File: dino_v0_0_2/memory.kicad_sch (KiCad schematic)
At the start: 15 parts, among them U19 74LS245, U21 74LS245, U24 AT28C256, U26 MCM60256AP, U51 7400, U74 74LS00, U75 74LS32

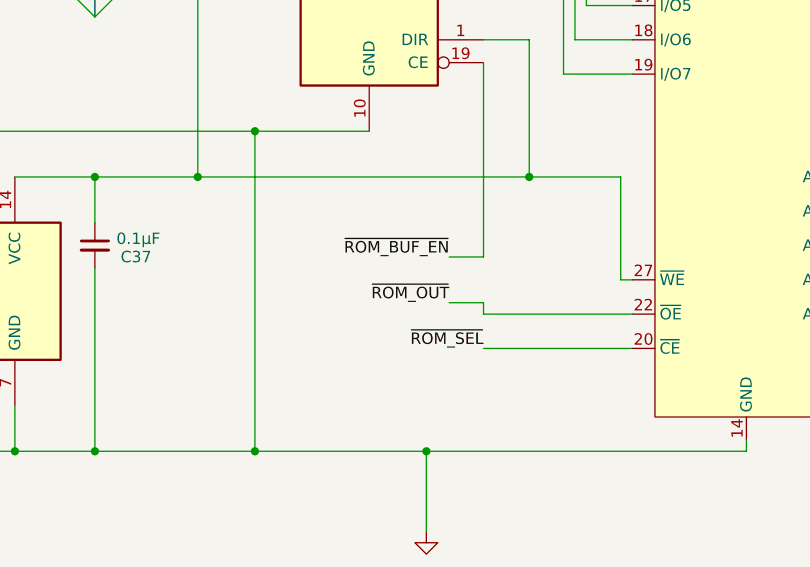
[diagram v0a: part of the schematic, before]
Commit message: feat: phase G_0 on silicon -- ROM readable as data, monitor runs its session
Three re-sourced pins make ROM readable as data (PROG_test3 0x4D, romsoak
0x00 over 65536 reads). The monitor then runs the session from the ask:
D 0000 -> 0x11, W FF00,99 -> 0x99, D FF00 -> 0x99, O FF00 on OB.

Four faults sat between the copper and that session, all fixed, all in
.git/sdd/PHASE_G_0.md RESULTS:

1. U15 (microcode EEPROM, CW8-15) pulsed END on its own for ~25ns with a
   static address, clean rails and ~OE/~CE low, locked to no clock in the
   machine. U61 turned it into ~MR low, U6 cleared T under HALT, and the
   byte behind the HALT ran. Every "HALT escape" ever recorded was this.
   Chip replaced; same image; no pulses.
2. MVI/MVIX/MVIS parked the immediate on a bus fight: CW14 flipped M to
   MAR before the source decode retired ~ROM_OUT, FETCH_RAM fired, and the
   RAM drove the cell's old byte under U18's open latch. PROG_isa was blind
   to it (PLANT rewrites the same 0x2E). Settle row with pc_up on the
   settle, not the park. Burned: U9 0xC52B  U15 0xDCD1  U23 0xCB8E.
3. LE_MDR opened on ~RAM_LOAD during the replay row. U39.4 strapped +5V;
   LE_MDR = NOT(READS_IDLE).
4. The spec's RAM-side wire (U74.9 <- READ) was identical logic and three
   gates faster on M15, which made fault 2 deterministic. Reverted to
   RAM_OE_ON.

Schematic matches copper: --since HEAD reads copper 3 (U22.11, U24.22,
U39.4), annotate 2; ERC delta -2, none new.

Tooling: asm/wander (ten slots, escape ladder), test4, test5 (six-slot
bisection), romsoak (ROM-as-data x65536, OB = misses), answer keys for
each; make gen-isa and burn-prog-isa; progrom_gen no longer writes over
asm-owned images; test_no_rom_park_flips_M_before_the_latch_closes.

OPEN: first ~3 data reads after POWER-UP miss, five witnesses in the doc.

Co-Authored-By: Claude Fable 5.1 <noreply@anthropic.com>
Claude-Session: https://claude.ai/code/session_01QTZogB99di5hEgzEycbhhD
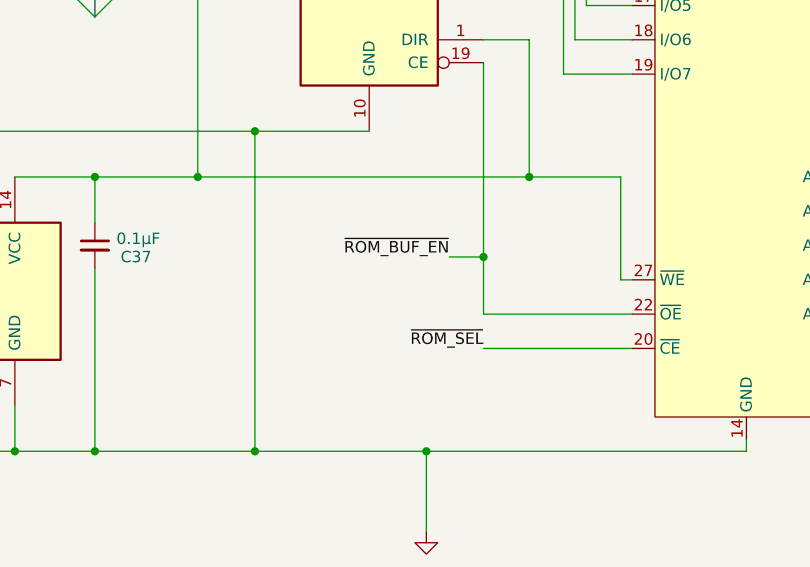
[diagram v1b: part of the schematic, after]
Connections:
- net ~{ROM_OUT} is gone; now on net ~{ROM_BUF_EN}: U24.22 (~{OE})
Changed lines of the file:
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@@
+	)
+	(junction
+		(at 200.66 90.17)
+		(diameter 0)
+		(color 0 0 0 0)
 	)
 	(junction
@@
 	(wire
 		(pts
-			(xy 196.85 95.25) (xy 200.66 95.25)
-		)
-		(stroke
-			(width 0)
-			(type default)
-		)
-	)
-	(wire
-		(pts
 			(xy 100.33 62.23) (xy 105.41 62.23)
 		)
@@
 	(wire
 		(pts
-			(xy 200.66 95.25) (xy 200.66 96.52)
+			(xy 200.66 90.17) (xy 200.66 96.52)
 		)
 		(stroke
@@
 		)
 	)
+	(label "RAM_OE_ON"
+		(at 26.67 175.26 180)
+		(effects
+			(font
+				(size 1.27 1.27)
+			)
+			(justify right bottom)
+		)
+	)
 	(label "MDR1"
 		(at 160.02 45.72 0)
@@
 		)
 	)
-	(label "~{ROM_OUT}"
-		(at 196.85 95.25 180)
-		(effects
-			(font
-				(size 1.27 1.27)
-			)
-			(justify right bottom)
-		)
-	)
 	(label "MDR5"
 		(at 154.94 55.88 180)
@@
 		(effects
 			(font
-				(size 1.27 1.27)
-			)
-			(justify right bottom)
-		)
-	)
-	(label "RAM_OE_ON"
-		(at 26.67 175.26 180)
-		(effects
-			(font

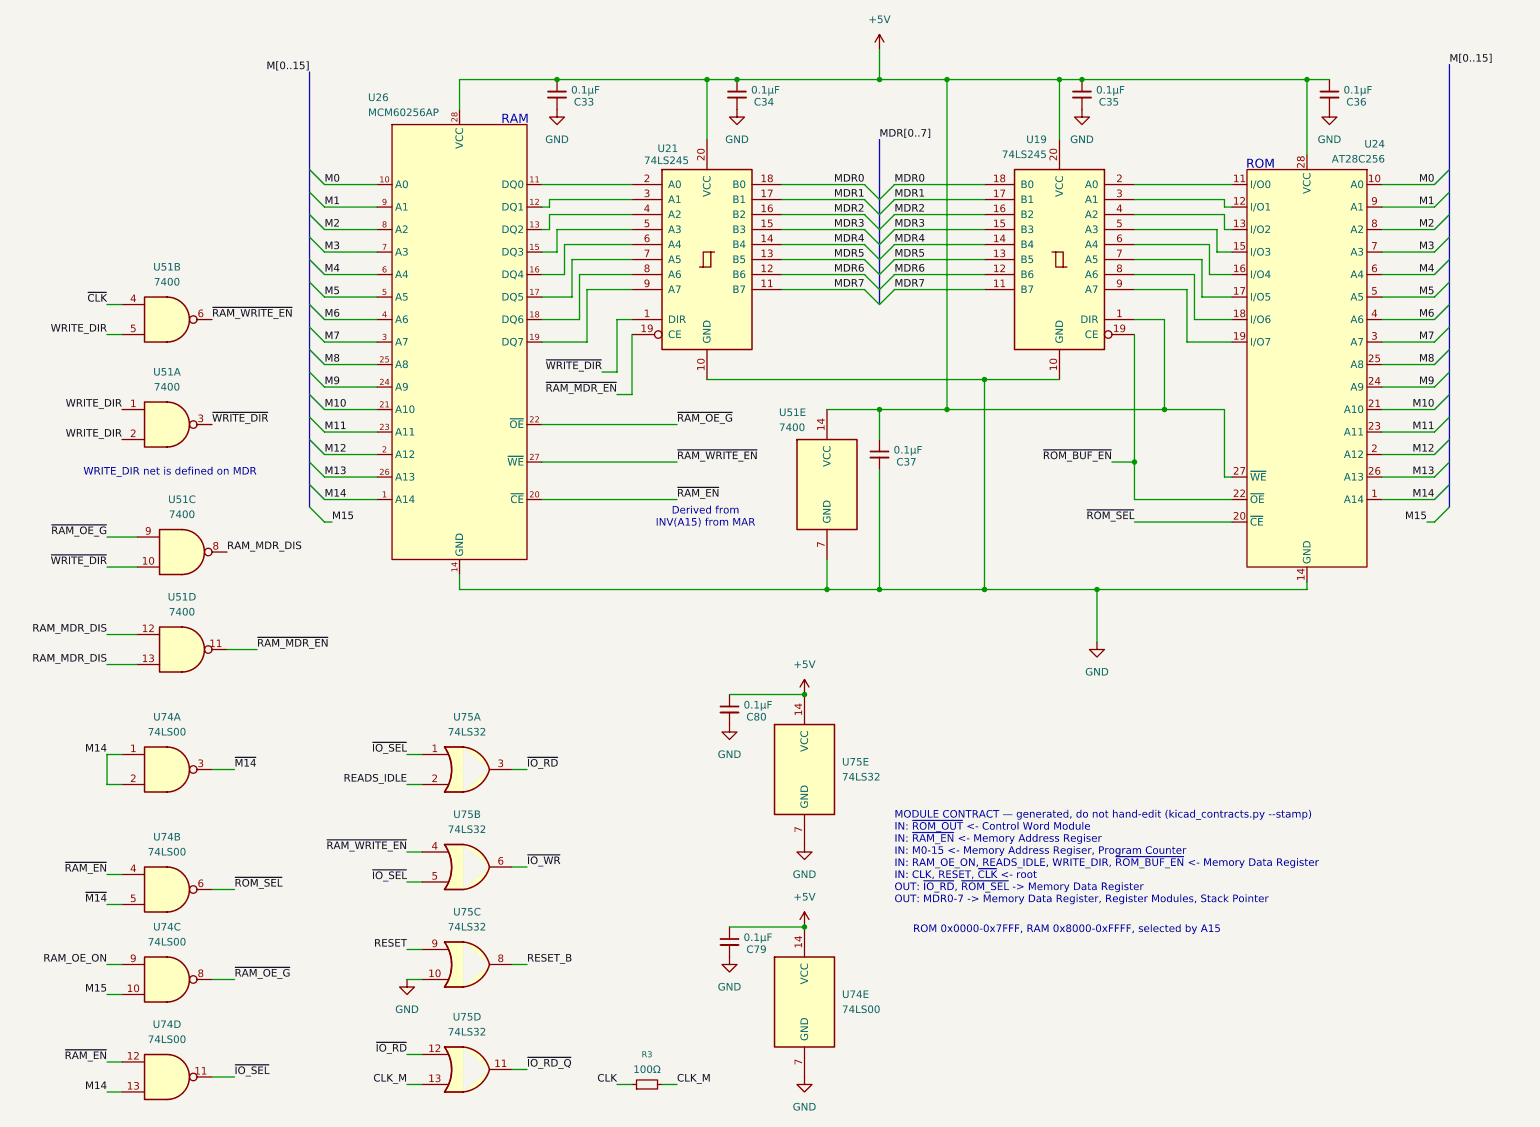
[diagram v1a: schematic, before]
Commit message: feat(kicad): footprints, power sheet, global labels, PCB draft
Every symbol gets a stock THT footprint (plain DIP, no sockets, so the
3D render shows ICs). New Power sheet: 24-pin ATX header for a picoPSU,
rails +5V/+3.3V/+12V/-12V/GND only; no -5V exists on any ATX unit since
2003, none drawn. PS_ON# on a 2-pin header.

Cross-sheet labels become global labels. KiCad joined nothing between
sheets before: 122 base names were split per sheet, ERC saw 90 undriven
inputs whose driver sat one sheet away, and the PCB ratsnest stopped at
every sheet boundary. Proof: KiCad's netlist after equals a name-join of
its netlist before plus the 15 CW alias pairs, pin for pin.

kicad_contracts took a node's sheet from the net name's /Sheet/ prefix;
global nets have none, so it emitted an empty contracts doc. Sheet now
comes from the component's own path; the doc regenerates with zero diff.

ERC 477 -> 2. Real fixes: ROM I/O pins input -> tri_state, '382 GND pin
power_out -> power_in, four orphan symbols rehomed to project lib `dino`,
one stub wire. 133 by-design warnings excluded by uuid ('245 readback on
counter Q, alias stubs, probe-point labels); the two left are bus
signals the peripheral bus sheet will consume.

PCB draft: 198 footprints placed per sheet, all pads netted, no tracks.

Co-Authored-By: Claude Fable 5.1 <noreply@anthropic.com>
Claude-Session: https://claude.ai/code/session_018irreFHb1xEykW5kCD26ow
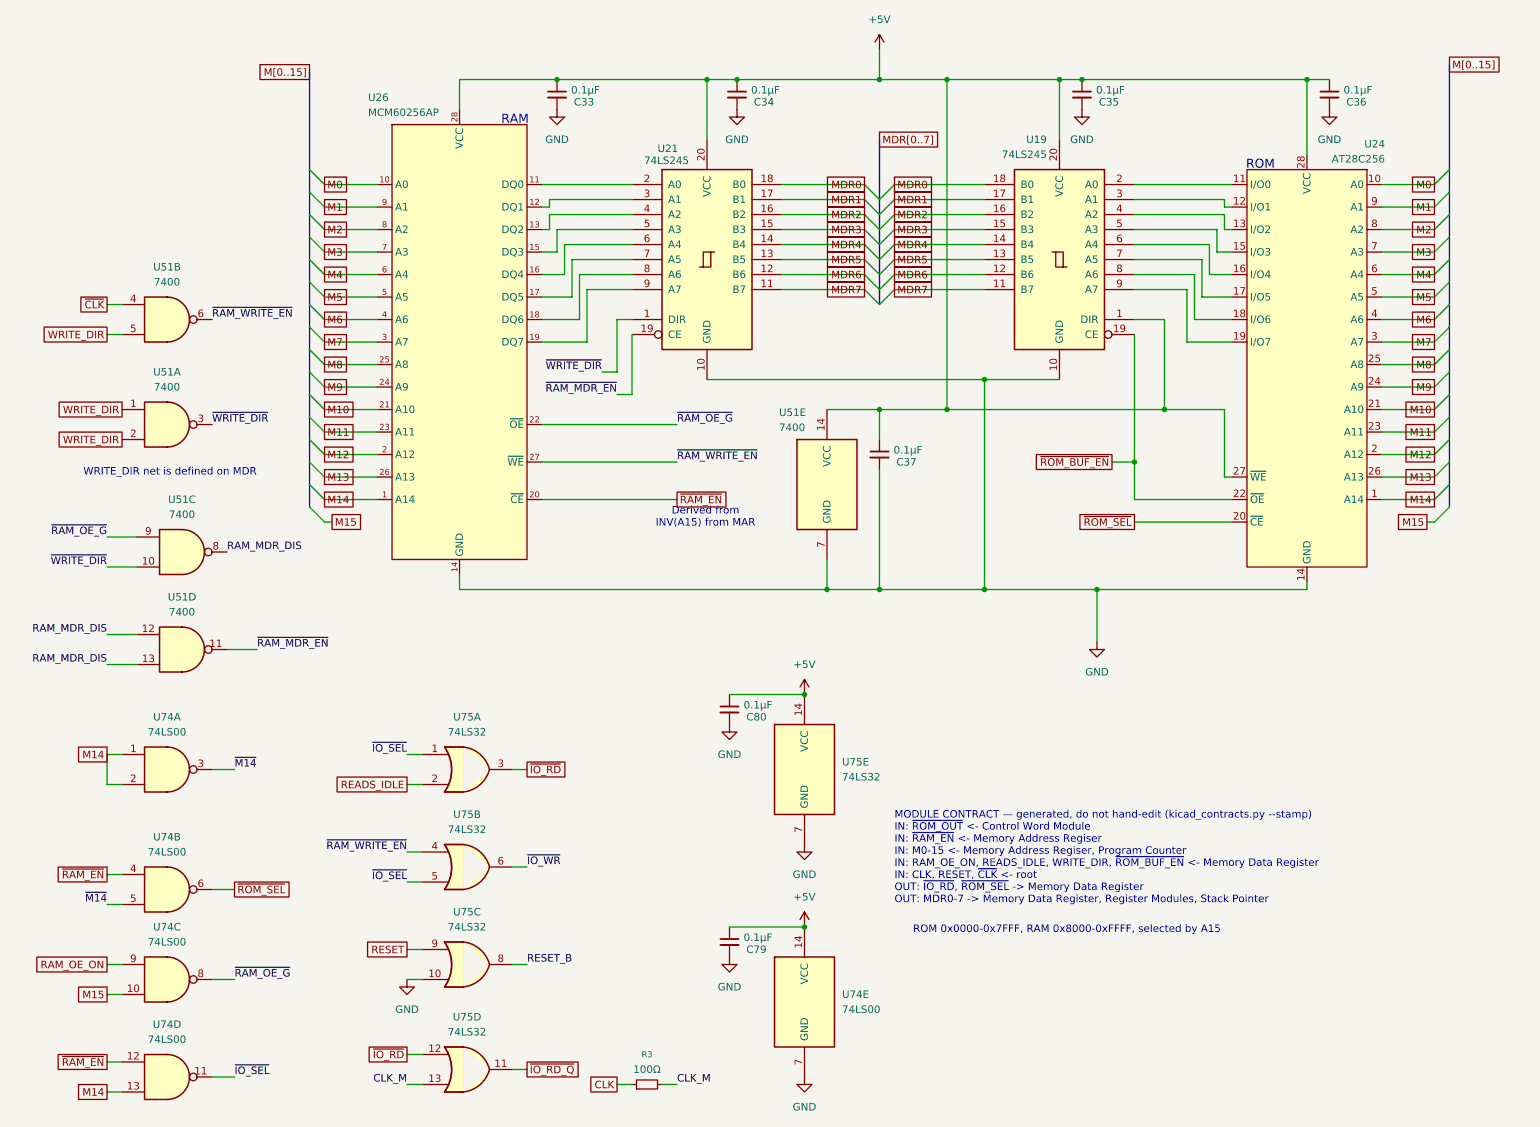
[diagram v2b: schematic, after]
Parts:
- C33, C34, C35, C36, C37, C79, C80: footprint (none) -> Capacitor_THT:C_Disc_D5.0mm_W2.5mm_P2.50mm
- R3: footprint (none) -> Resistor_THT:R_Axial_DIN0207_L6.3mm_D2.5mm_P10.16mm_Horizontal
- U19, U21: footprint (none) -> Package_DIP:DIP-20_W7.62mm
- U24: footprint (none) -> Package_DIP:DIP-28_W15.24mm; symbol Memory_EEPROM:AT28C256 -> dino:AT28C256
- U26: footprint (none) -> Package_DIP:DIP-28_W15.24mm; symbol Memory_RAM:MCM60256AP -> dino:MCM60256AP
- U51, U74, U75: footprint (none) -> Package_DIP:DIP-14_W7.62mm

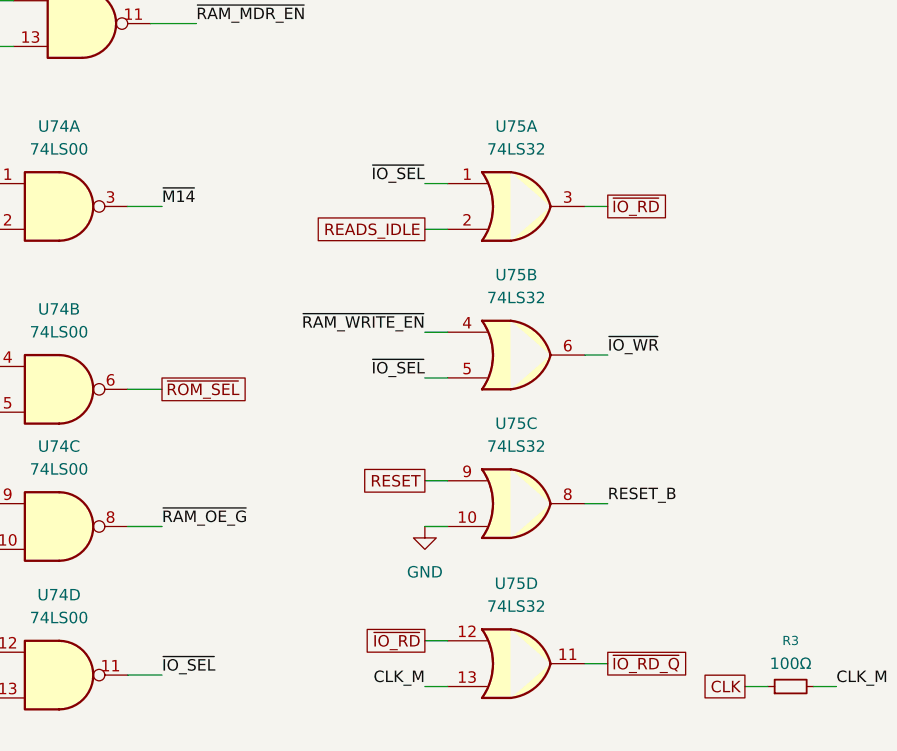
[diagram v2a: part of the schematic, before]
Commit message: feat(kicad): peripheral bus sheet, dino_io card project, dino_bus lib
Eight 2x25 0.1in card-edge sockets on the core (peripheral_bus.kicad_sch,
J1-J8) bussed on global labels; U78 '04 buffers ~{CLK} into CLK_B so no
card sees U27.5 raw; ~{IRQ} ~{NMI} ~{DMARQ} ~{DMAAK} RDY named and
reserved, spares no-connected. Rails are what the picoPSU delivers.

Card zero leaves the core: the Input sheet becomes dino_io/, references
unchanged, plus edge connector J1. input_output.kicad_sch is now
front_panel.kicad_sch: the OB LEDs are the OUT register's display, not a
card, and the W park stays at the origin (PHASE_E).

dino_bus/ is generated from one pin table in bus_gen.py: both symbol
flavours, the finger footprint, and a placeholder socket footprint until
a part is chosen. Edge-side pins carry direction types so a card project
passes ERC alone; socket side is passive.

Proof: core and card netlists joined through the slot-0 pin numbers
partition every pre-existing pin exactly as the core did before the
split. ERC 0/0 on both projects. dino_serial not yet given its J2.

Co-Authored-By: Claude Fable 5.1 <noreply@anthropic.com>
Claude-Session: https://claude.ai/code/session_018irreFHb1xEykW5kCD26ow
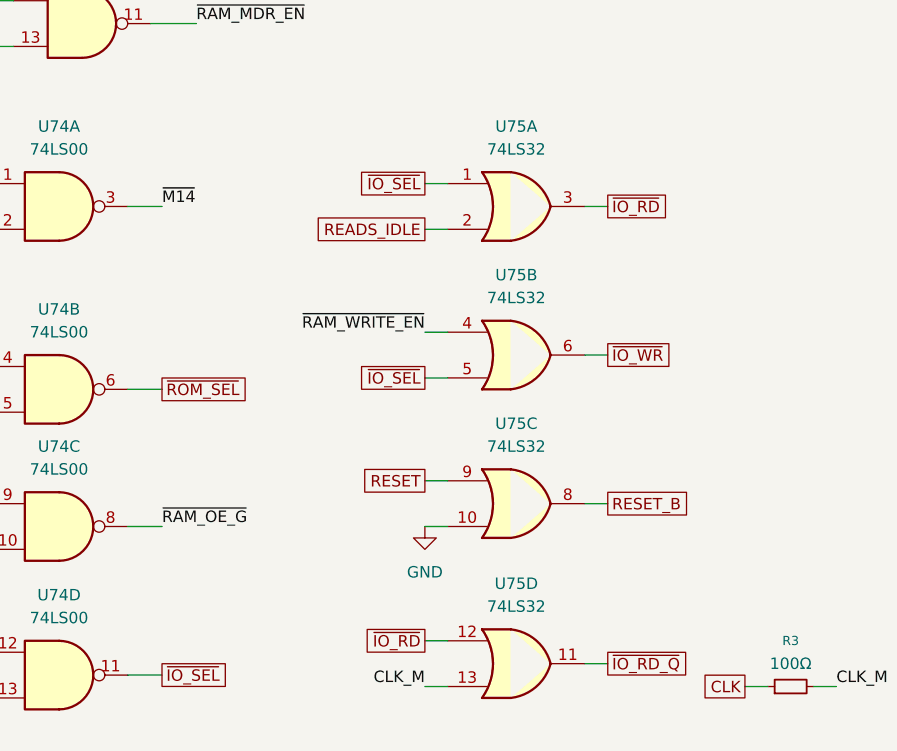
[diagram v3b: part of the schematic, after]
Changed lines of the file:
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@@
 		)
 	)
-	(label "~{IO_SEL}"
+	(global_label "~{IO_SEL}"
+		(shape passive)
 		(at 77.47 161.29 180)
-		(effects
-			(font
-				(size 1.27 1.27)
-			)
-			(justify right bottom)
+		(fields_autoplaced yes)
+		(effects
+			(font
+				(size 1.27 1.27)
+			)
+			(justify right)
+		)
+		(property "Intersheetrefs" "${INTERSHEET_REFS}"
+			(at 77.47 161.29 180)
+			(hide yes)
+			(effects
+				(font
+					(size 1.27 1.27)
+				)
+				(justify right)
+			)
 		)
 	)
@@
 		)
 	)
-	(label "~{IO_SEL}"
+	(global_label "~{IO_SEL}"
+		(shape passive)
 		(at 77.47 139.7 180)
-		(effects
-			(font
-				(size 1.27 1.27)
-			)
-			(justify right bottom)
+		(fields_autoplaced yes)
+		(effects
+			(font
+				(size 1.27 1.27)
+			)
+			(justify right)
+		)
+		(property "Intersheetrefs" "${INTERSHEET_REFS}"
+			(at 77.47 139.7 180)
+			(hide yes)
+			(effects
+				(font
+					(size 1.27 1.27)
+				)
+				(justify right)
+			)
 		)
 	)
@@
 		)
 	)
-	(label "~{IO_WR}"
+	(global_label "~{IO_WR}"
+		(shape passive)
 		(at 97.79 158.75 0)
-		(effects
-			(font
-				(size 1.27 1.27)
-			)
-			(justify left bottom)
+		(fields_autoplaced yes)
+		(effects
+			(font
+				(size 1.27 1.27)
+			)
+			(justify left)
+		)
+		(property "Intersheetrefs" "${INTERSHEET_REFS}"
+			(at 97.79 158.75 0)
+			(hide yes)
+			(effects
+				(font
+					(size 1.27 1.27)
+				)
+				(justify left)
+			)
 		)
 	)
@@
 		)
 	)
-	(label "~{IO_SEL}"
+	(global_label "~{IO_SEL}"
+		(shape passive)
 		(at 48.26 194.31 0)
-		(effects
-			(font
-				(size 1.27 1.27)
-			)
-			(justify left bottom)
+		(fields_autoplaced yes)
+		(effects
+			(font
+				(size 1.27 1.27)
+			)
+			(justify left)
+		)
+		(property "Intersheetrefs" "${INTERSHEET_REFS}"
+			(at 48.26 194.31 0)
+			(hide yes)
+			(effects
+				(font
+					(size 1.27 1.27)
+				)
+				(justify left)
+			)
 		)
 	)
@@
 		)
 	)
-	(label "RESET_B"
+	(global_label "RESET_B"
+		(shape passive)
 		(at 97.79 175.26 0)
-		(effects
-			(font
-				(size 1.27 1.27)
-			)
-			(justify left bottom)
-		)
-	)
+		(fields_autoplaced yes)
+		(effects
+			(font
+				(size 1.27 1.27)
+			)
+			(justify left)
+		)
+		(property "Intersheetrefs" "${INTERSHEET_REFS}"
+			(at 97.79 175.26 0)
+			(hide yes)
+			(effects
+				(font
+					(size 1.27 1.27)
+				)
+				(justify left)
+			)
+		)
+	)
